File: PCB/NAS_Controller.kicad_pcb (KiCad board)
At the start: 4 copper layers, 119.5 x 99.6 mm, 1066 parts, among them J1 Barrel_Jack, J10 Conn_01x10, J11 10103594-0001LF, J12 Conn_01x03, J13 Conn_01x03, J14 20021121-00020C4LF, J15 Conn_01x03, J16 Conn_01x03, J17 Conn_01x03, J18 M20-9990246, J19 Conn_01x03, J2 Conn_01x04, J20 Conn_01x03, J3 105133-0011, J4 10103594-0001LF, J5 NPPN101BFCN-RC, J6 NPPN101BFCN-RC, J7 Conn_01x03, J8 PPTC081LFBN-RC, J9 PPTC081LFBN-RC, Q1 DMN6068LK3-13, Q10 AOD409, Q11 DMG1026UV-7, Q12 DMN6068LK3-13, Q13 DMN6068LK3-13, Q2 DMN6068LK3-13, Q3 MMBT3904-TP, Q4 2N7002, Q5 2N7002, Q6 2N7002, Q7 DMN6068LK3-13, Q8 AOD409, Q9 AOD409, SW1 SW_SP3T_1COM_234, U1 ZXCT1110, U10 TS5A3357DCUR, U11 PCA6416APW,118, U12 ZXGD3009E6TA, U13 TS462CDT, U14 AP65211AWU-7, U15 RT7258GSP, U16 RT7258GSP, U17 LM3481MM, U18 TS462CDT, U19 TS5A3357DCUR, U2 TS462CDT, U3 AZ1084CD-3.3, U4 TS462CDT, U5 TS462CDT, U6 TMS320F28035PAGS, U7 MB85RS16, U8 CY7C65634-48AXCT, U9 TS5A3357DCUR, Y1 12MHz

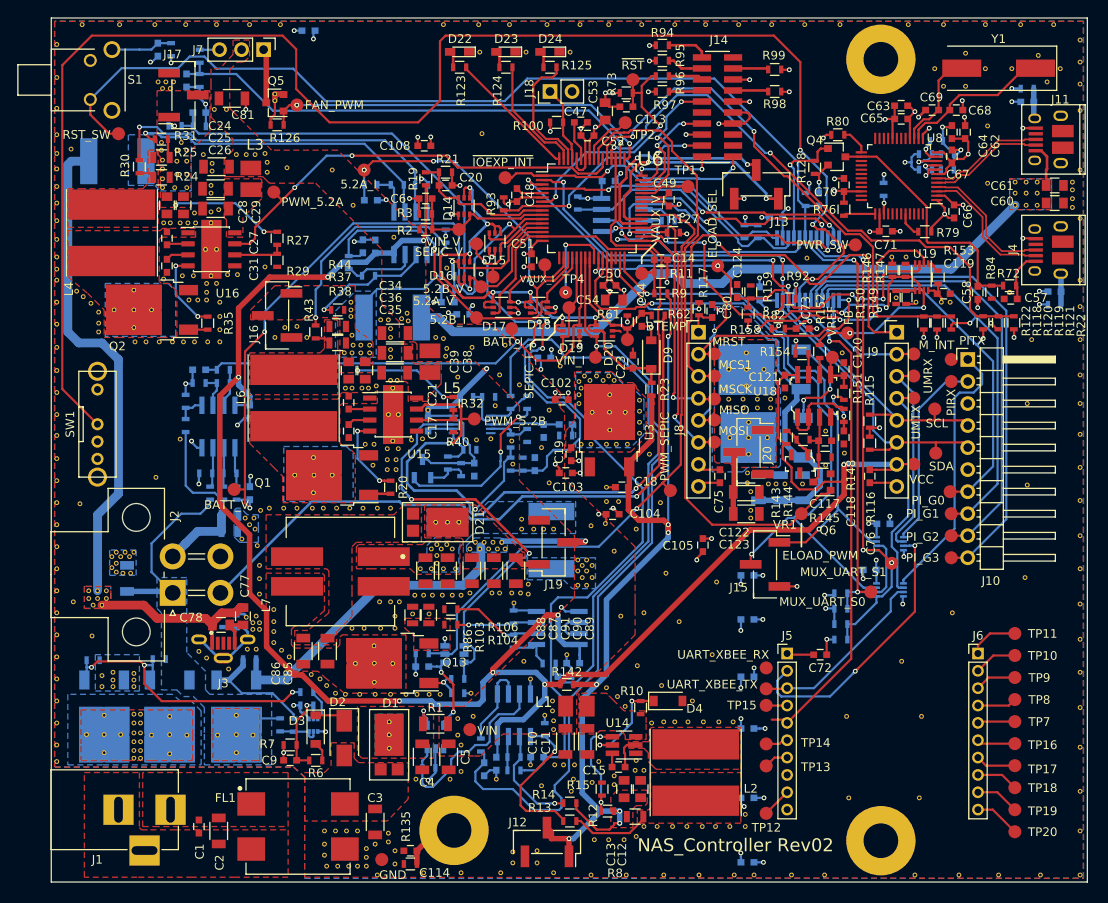
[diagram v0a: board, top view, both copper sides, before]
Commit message: Moved components & copper away from mtg holes.
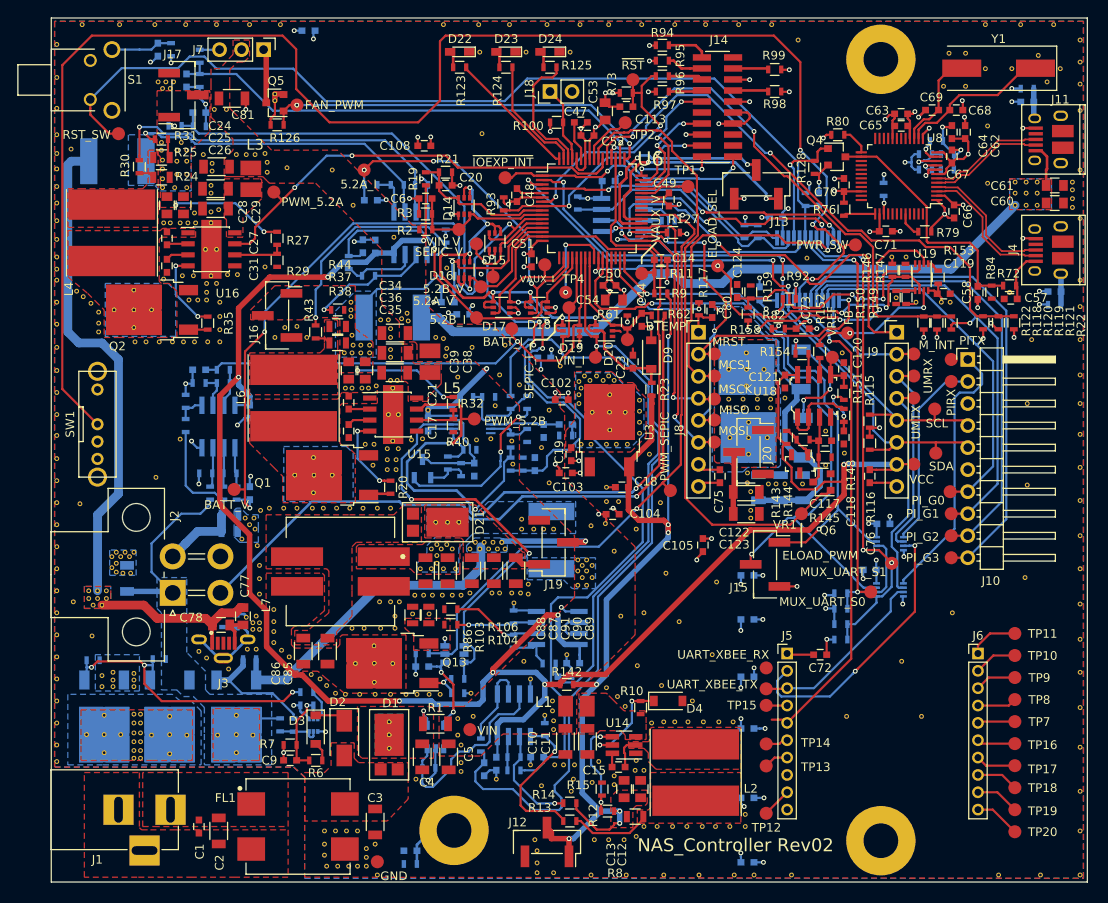
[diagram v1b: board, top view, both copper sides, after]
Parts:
- removed the REF** at (100.1, 89.9)
- removed the REF** at (91.9, 89.9)
- removed the REF** at (42.9, 98.6)
- removed the REF** at (47.2, 98.6)
- removed the REF** at (51.8, 98.6)
- removed the REF** at (89.2, 98.8)
- removed the REF** at (99.6, 98.8)
- removed the REF** at (104.6, 98.8)
- removed the REF** at (102.9, 0.76)
- removed the REF** at (98.8, 0.76)
- removed the REF** at (90.9, 0.76)
- removed the REF** at (38.9, 95.0)
- removed the REF** at (38.9, 94.0)
- removed the REF** at (39.6, 96.0)
- removed the REF** at (39.6, 97.5)
- C114, R135: moved to B.Cu
- moved REF** 3.02 mm to (56.0, 98.6)
- moved REF** 2.90 mm to (55.8, 94.7)
- moved REF** 2.43 mm to (103.5, 4.06)
- moved REF** 2.29 mm to (47.2, 85.9)
- moved REF** 1.93 mm to (86.1, 2.54)
- moved C63 0.94 mm to (98.0, 11.0)
- moved C65 0.81 mm to (98.0, 12.4)
- moved GND 0.57 mm to (37.6, 97.3)
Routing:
- net +3V3: track 113.7 -> 114.5 mm
- net GND: track 208.9 -> 208.3 mm

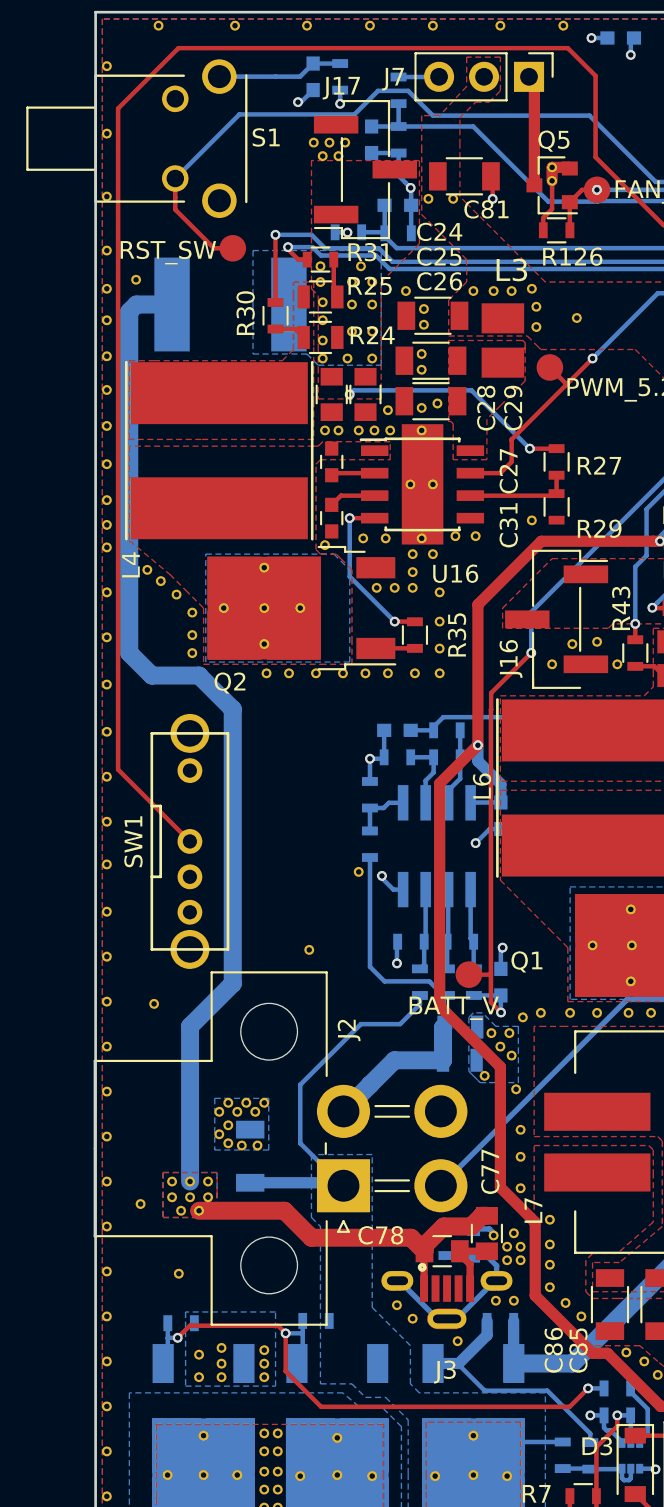
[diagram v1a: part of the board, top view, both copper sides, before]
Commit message: Updated switch, need to re-position for alignment...
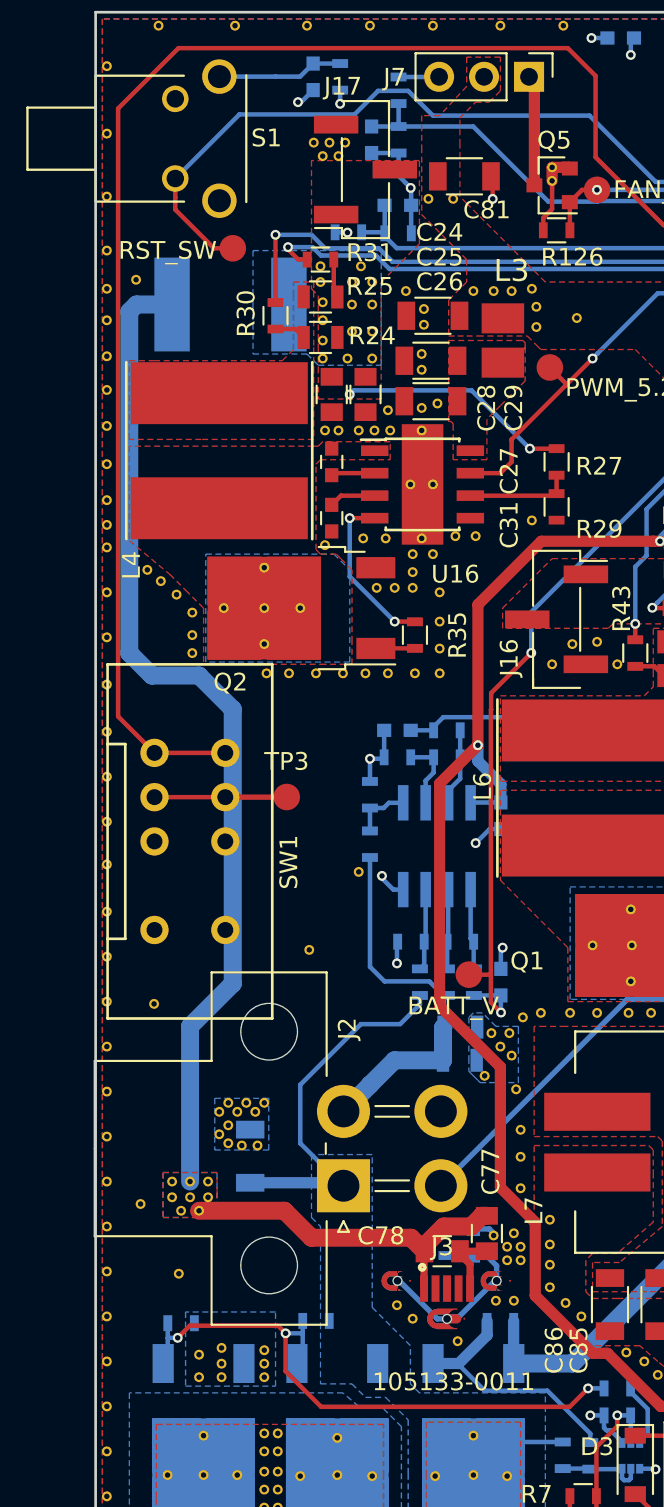
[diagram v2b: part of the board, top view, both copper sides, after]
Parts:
- added TP3: TEST, Measurement_Points:Measurement_Point_Round-SMD-Pad_Small, F.Cu at (10.8, 44.3)
- J3: footprint 105133-0011_FixedHoles:MOLEX_105133-0011 -> 105133-0011:MOLEX_105133-0011
- SW1: value SW_SP3T_1COM_234 -> EG2322; footprint CustomFootprints:OS103011MA7QP1 -> CustomFootprints:EG2322
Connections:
- SW1 pad 1: GND -> PWR_SW_IN
- SW1 pad 2: PWR_SW_IN -> Net-(SW1-Pad2)
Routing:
- net Net-(SW1-Pad2): track 0.00 -> 7.47 mm
- net PWR_SW_IN: track 187.6 -> 185.8 mm
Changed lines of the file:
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@@
 (kicad_pcb (version 4) (host pcbnew 4.0.7)
   (general
-    (links 1571)
-    (no_connects 11)
-    (area -8.97681 -1.56538 122.532325 101.23342)
+    (links 1561)
+    (no_connects 19)
+    (area -0.075001 -0.075001 119.525001 99.693801)
     (thickness 1.6)
     (drawings 17)
-    (tracks 3041)
+    (tracks 3045)
     (zones 0)
-    (modules 1051)
-    (nets 260)
+    (modules 1052)
+    (nets 261)
   )
   (page A4)
@@
   (net 258 "Net-(R154-Pad2)")
   (net 259 "Net-(VR1-Pad3)")
+  (net 260 "Net-(SW1-Pad2)")
   (net_class Default "This is the default net class."
     (clearance 0.1524)
@@
     (add_net "Net-(R81-Pad1)")
     (add_net "Net-(R92-Pad1)")
+    (add_net "Net-(SW1-Pad2)")
     (add_net "Net-(TP1-Pad1)")
     (add_net "Net-(TP2-Pad1)")
@@
       (net 30 "Net-(C56-Pad1)"))
   )
-  (module CustomFootprints:OS103011MA7QP1 (layer F.Cu)
-    (at 5.325 46.8326 270)
-    (fp_text reference SW1 (at 0 3.15 270) (layer F.SilkS)
-      (effects (font (size 1 1) (thickness 0.15)))
-    )
-    (fp_text value SW_SP3T_1COM_234 (at 0 -3.1 270) (layer F.Fab)
-      (effects (font (size 1 1) (thickness 0.15)))
-    )
-    (fp_line (start -2 2.15) (end -2 1.65) (layer F.SilkS) (width 0.15))
-    (fp_line (start -2 1.65) (end 2 1.65) (layer F.SilkS) (width 0.15))
-    (fp_line (start 2 1.65) (end 2 2.15) (layer F.SilkS) (width 0.15))
-    (fp_line (start -6.1 -2.15) (end 6.1 -2.15) (layer F.SilkS) (width 0.15))
-    (fp_line (start 6.1 -2.15) (end 6.1 2.15) (layer F.SilkS) (width 0.15))
-    (fp_line (start 6.1 2.15) (end -6.1 2.15) (layer F.SilkS) (width 0.15))
-    (fp_line (start -6.1 2.15) (end -6.1 -2.15) (layer F.SilkS) (width 0.15))
-    (pad 4 thru_hole circle (at 4 0 270) (size 1.4 1.4) (drill 0.8) (layers *.Cu *.Mask)
-      (net 4 GND))
-    (pad 3 thru_hole circle (at 2 0 270) (size 1.4 1.4) (drill 0.8) (layers *.Cu *.Mask)
-      (net 4 GND))
-    (pad 2 thru_hole circle (at 0 0 270) (size 1.4 1.4) (drill 0.8) (layers *.Cu *.Mask)
-      (net 36 PWR_SW_IN))
-    (pad MTG thru_hole circle (at 6.1 0 270) (size 2.2 2.2) (drill 1.5) (layers *.Cu *.Mask))
-    (pad MTG thru_hole circle (at -6.1 0 270) (size 2.2 2.2) (drill 1.5) (layers *.Cu *.Mask))
-    (pad 1 thru_hole circle (at -4 0 270) (size 1.4 1.4) (drill 0.8) (layers *.Cu *.Mask)
-      (net 4 GND))
-  )
   (module Resistors_SMD:R_0603 (layer F.Cu)
     (at 26.03502 12.31902 180)
@@
     (pad 1 smd circle (at 0 0) (size 1.5 1.5) (layers F.Cu F.Mask))
   )
-  (module 105133-0011_FixedHoles:MOLEX_105133-0011 (layer F.Cu)
+  (module 105133-0011:MOLEX_105133-0011 (layer F.Cu)
     (at 19.84802 71.64702)
     (descr "Conn Micro USB Type B RCP 5 POS 0.65mm Solder ST SMD 5 Terminal 1 Port Embossed T/R")
     (attr smd)
-    (fp_text reference J3 (at -0.036 5.061) (layer F.SilkS)
-      (effects (font (size 1.00171 1.00171) (thickness 0.15)))
+    (fp_text reference J3 (at -0.26046 -1.90826) (layer F.SilkS)
+      (effects (font (size 1.00171 1.00171) (thickness 0.05)))
     )
-    (fp_text value 105133-0011 (at 0.375033 5.71529) (layer F.SilkS) hide
+    (fp_text value 105133-0011 (at 0.375033 5.71529) (layer F.SilkS)
       (effects (font (size 1.00005 1.00005) (thickness 0.05)))
     )
@@
     (pad 5 smd rect (at 1.3 0.44 90) (size 1.5 0.45) (layers F.Cu F.Paste F.Mask)
       (net 4 GND))
-    (pad 6 thru_hole oval (at 0 2.15 90) (size 1.09982 2.199894) (drill oval 0.5 1.6002) (layers *.Cu *.Mask)
+    (pad 6 smd rect (at 0.98 2.14) (size 0.1 0.1) (layers F.Cu F.Paste F.Mask)
       (net 164 "Net-(C79-Pad2)"))
-    (pad 7 thru_hole oval (at -2.8 0 90) (size 1.09982 1.800098) (drill oval 0.5 1.199896) (layers *.Cu *.Mask)
+    (pad Hole np_thru_hole circle (at 0 2.15) (size 0.5 0.5) (drill 0.5) (layers))
+    (pad Hole np_thru_hole circle (at -2.8 0) (size 0.5 0.5) (drill 0.5) (layers))
+    (pad 7 smd rect (at -2.09 0) (size 0.1 0.1) (layers F.Cu F.Paste F.Mask)
       (net 164 "Net-(C79-Pad2)"))
-    (pad 8 thru_hole oval (at 2.8 0 90) (size 1.09982 1.800098) (drill oval 0.5 1.199896) (layers *.Cu *.Mask)
+    (pad Hole np_thru_hole circle (at 2.8 0) (size 0.5 0.5) (drill 0.5) (layers))
+    (pad 8 smd rect (at 3.56 0) (size 0.1 0.1) (layers F.Cu F.Paste F.Mask)
       (net 164 "Net-(C79-Pad2)"))
   )
+  (module CustomFootprints:EG2322 (layer F.Cu)
+    (at 5.325 46.8326 270)
+    (fp_text reference SW1 (at 1.17342 -5.59702 270) (layer F.SilkS)
+      (effects (font (size 1 1) (thickness 0.15)))
+    )
+    (fp_text value " EG2322" (at -0.05 -5.5 270) (layer F.Fab)
+      (effects (font (size 1 1) (thickness 0.15)))
+    )
+    (fp_line (start -5.5 3.65) (end -5.5 4.65) (layer F.SilkS) (width 0.15))
+    (fp_line (start -5.5 3.65) (end 5.5 3.65) (layer F.SilkS) (width 0.15))
+    (fp_line (start 5.5 3.65) (end 5.5 4.65) (layer F.SilkS) (width 0.15))
+    (fp_line (start -10 -4.65) (end 10 -4.65) (layer F.SilkS) (width 0.15))
+    (fp_line (start 10 -4.65) (end 10 4.65) (layer F.SilkS) (width 0.15))
+    (fp_line (start 10 4.65) (end -10 4.65) (layer F.SilkS) (width 0.15))
+    (fp_line (start -10 4.65) (end -10 -4.65) (layer F.SilkS) (width 0.15))
+    (pad 2 thru_hole circle (at -2.5 2 270) (size 1.6 1.6) (drill 0.9) (layers *.Cu *.Mask)
+      (net 260 "Net-(SW1-Pad2)"))
+    (pad 1 thru_hole circle (at -5 2 270) (size 1.6 1.6) (drill 0.9) (layers *.Cu *.Mask)
+      (net 36 PWR_SW_IN))
+    (pad 3 thru_hole circle (at 0 2 270) (size 1.6 1.6) (drill 0.9) (layers *.Cu *.Mask)
+      (net 4 GND))
+    (pad 4 thru_hole circle (at 5 2 270) (size 1.6 1.6) (drill 0.9) (layers *.Cu *.Mask)
+      (net 4 GND))
+    (pad 5 thru_hole circle (at -5 -2 270) (size 1.6 1.6) (drill 0.9) (layers *.Cu *.Mask)
+      (net 36 PWR_SW_IN))
+    (pad 6 thru_hole circle (at -2.5 -2 270) (size 1.6 1.6) (drill 0.9) (layers *.Cu *.Mask)
+      (net 260 "Net-(SW1-Pad2)"))
+    (pad 7 thru_hole circle (at 0 -2 270) (size 1.6 1.6) (drill 0.9) (layers *.Cu *.Mask)
+      (net 4 GND))
+    (pad 8 thru_hole circle (at 5 -2 270) (size 1.6 1.6) (drill 0.9) (layers *.Cu *.Mask)
+      (net 4 GND))
+  )
+  (module Measurement_Points:Measurement_Point_Round-SMD-Pad_Small (layer F.Cu)
+    (at 10.79502 44.32302)
+    (descr "Mesurement Point, Round, SMD Pad, DM 1.5mm,")
+    (tags "Mesurement Point Round SMD Pad 1.5mm")
+    (attr virtual)
+    (fp_text reference TP3 (at 0 -2) (layer F.SilkS)
+      (effects (font (size 1 1) (thickness 0.15)))
+    )
+    (fp_text value TEST (at 0 2) (layer F.Fab)
+      (effects (font (size 1 1) (thickness 0.15)))
+    )
+    (fp_circle (center 0 0) (end 1 0) (layer F.CrtYd) (width 0.05))
+    (pad 1 smd circle (at 0 0) (size 1.5 1.5) (layers F.Cu F.Mask)
+      (net 260 "Net-(SW1-Pad2)"))
+  )
   (gr_line (start 86.48702 58.29302) (end 86.48702 60.96002) (layer F.SilkS) (width 0.2))
   (gr_line (start 68.07202 27.55902) (end 68.07202 28.32102) (layer F.SilkS) (width 0.2))
@@
   (segment (start 101.20868 11.68402) (end 102.274618 10.618082) (width 0.254) (layer F.Cu) (net 35))
   (segment (start 102.274618 10.618082) (end 102.299618 10.618082) (width 0.254) (layer F.Cu) (net 35))
+  (segment (start 3.325 41.8326) (end 7.325 41.8326) (width 0.254) (layer F.Cu) (net 36))
+  (segment (start 1.27002 5.439032) (end 1.27002 39.77762) (width 0.254) (layer F.Cu) (net 36))
+  (segment (start 1.27002 39.77762) (end 3.325 41.8326) (width 0.254) (layer F.Cu) (net 36))
   (segment (start 86.36002 15.24002) (end 86.36002 5.08002) (width 0.254) (layer F.Cu) (net 36))
   (segment (start 44.811088 9.519515) (end 42.301583 12.02902) (width 0.254) (layer F.Cu) (net 36))
-  (segment (start 1.27002 42.77762) (end 5.325 46.8326) (width 0.254) (layer F.Cu) (net 36))
   (segment (start 86.36002 5.08002) (end 83.31202 2.03202) (width 0.254) (layer F.Cu) (net 36))
   (segment (start 32.075995 12.02902) (end 28.236223 8.189248) (width 0.254) (layer F.Cu) (net 36))
@@
   (segment (start 26.67002 2.03202) (end 4.677032 2.03202) (width 0.254) (layer F.Cu) (net 36))
   (segment (start 4.677032 2.03202) (end 1.27002 5.439032) (width 0.254) (layer F.Cu) (net 36))
-  (segment (start 1.27002 5.439032) (end 1.27002 42.77762) (width 0.254) (layer F.Cu) (net 36))
   (segment (start 92.71002 26.16202) (end 91.64936 26.16202) (width 0.254) (layer F.Cu) (net 36))
   (segment (start 91.64936 26.16202) (end 91.363821 26.447559) (width 0.254) (layer F.Cu) (net 36))
@@
   (segment (start 87.311827 41.119421) (end 87.311827 38.718421) (width 0.254) (layer F.Cu) (net 258))
   (segment (start 87.311827 38.718421) (end 87.299827 38.706421) (width 0.254) (layer F.Cu) (net 258))
+  (segment (start 3.325 44.3326) (end 7.325 44.3326) (width 0.254) (layer F.Cu) (net 260))
+  (segment (start 7.325 44.3326) (end 10.78544 44.3326) (width 0.3048) (layer F.Cu) (net 260))
+  (segment (start 10.78544 44.3326) (end 10.79502 44.32302) (width 0.3048) (layer F.Cu) (net 260))
   (zone (net 2) (net_name "Net-(C1-Pad1)") (layer F.Cu) (hatch edge 0.508)
     (priority 1)
